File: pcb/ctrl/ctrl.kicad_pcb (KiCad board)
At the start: 2 copper layers, 50 x 50 mm, 16 parts, among them SW1 SW_Push, U1 ArduinoProMicro

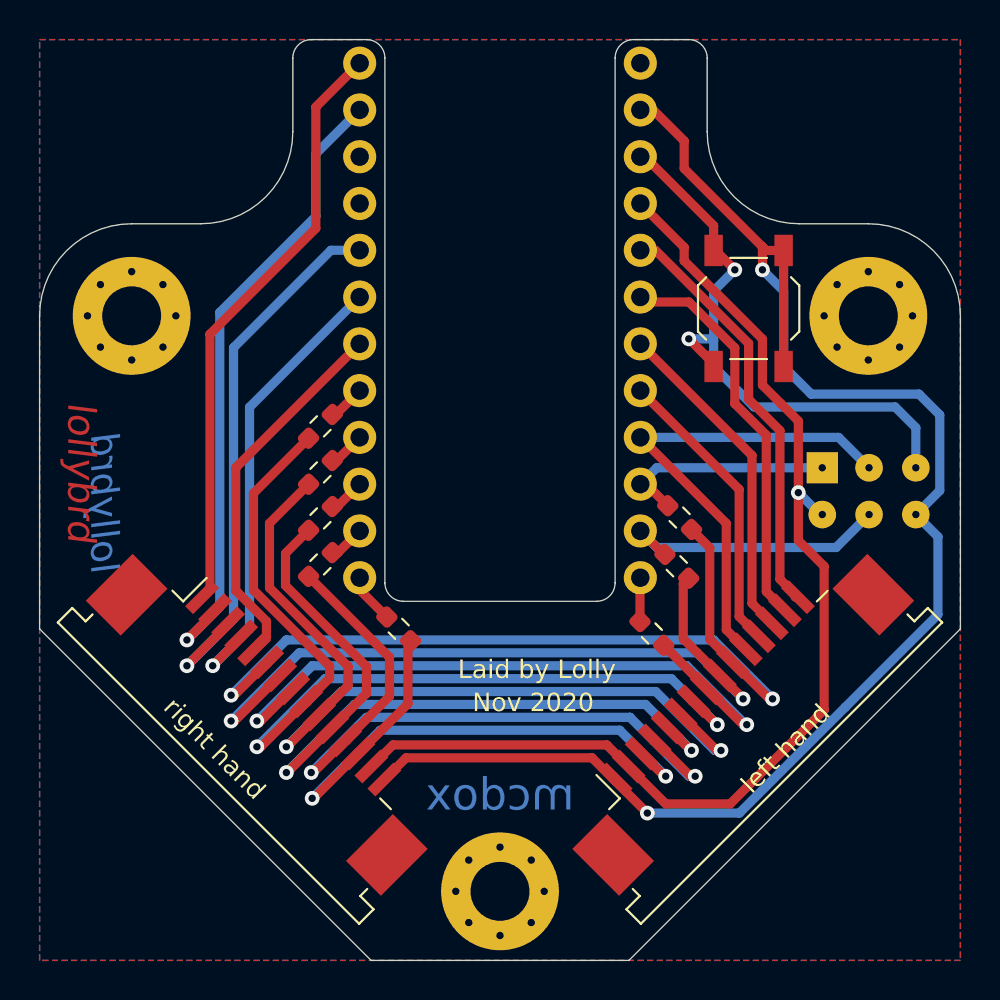
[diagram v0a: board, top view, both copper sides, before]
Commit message: case PCB and outline placement.
Can fit all 5 layers on a single 400x600mm sheet.
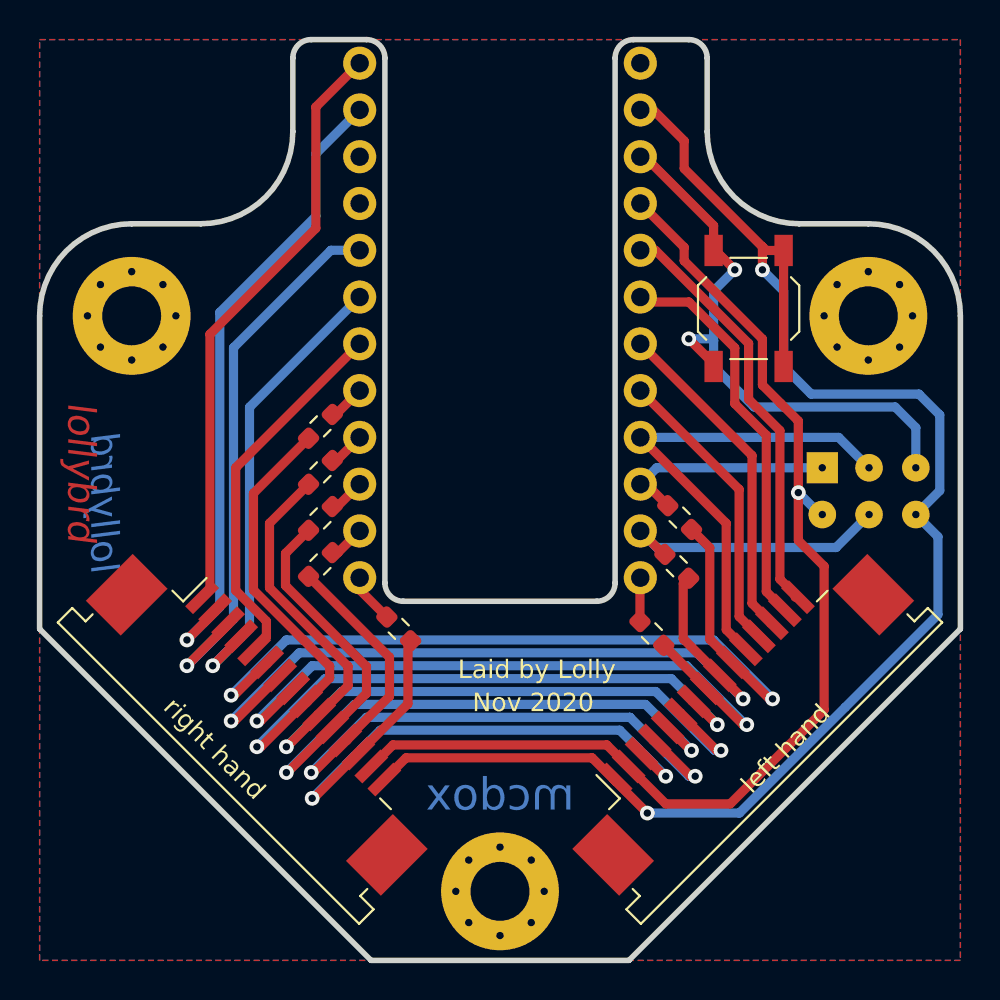
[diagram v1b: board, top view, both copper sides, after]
